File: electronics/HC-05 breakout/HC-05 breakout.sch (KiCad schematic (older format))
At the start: 11 parts, among them SW1 AT?, U1 AMS1117, U2 HC-05

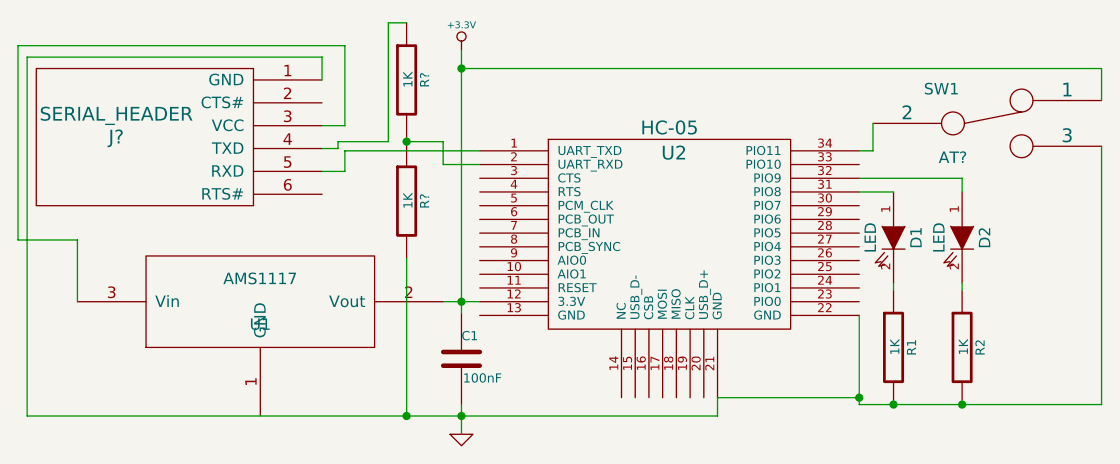
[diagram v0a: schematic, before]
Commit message: annotated hc-05 breakout
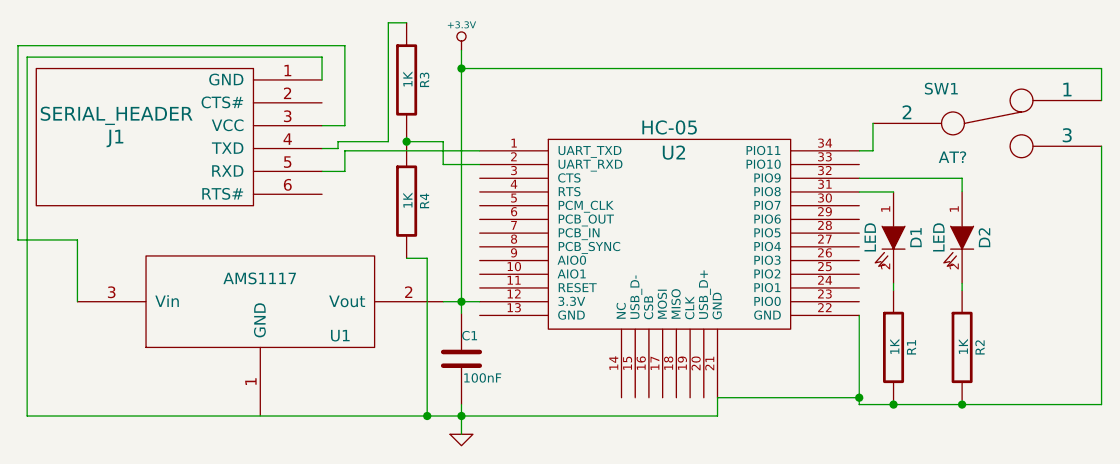
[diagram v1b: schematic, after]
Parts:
- gave numbers to parts that had none: 3
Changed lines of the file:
@@
-$EndComp
-$Comp
-L AMS1117 U1
-U 1 1 533D0877
-P 1900 2220
-F 0 "U1" H 1900 2120 50  0000 C CNN
-F 1 "AMS1117" H 1900 2320 50  0000 C CNN
-F 2 "" H 1900 2220 60  0000 C CNN
-F 3 "" H 1900 2220 60  0000 C CNN
-	1    1900 2220
-	1    0    0    -1
 $EndComp
 $Comp
@@
 Connection ~ 2780 1200
 $Comp
-L SERIAL_HEADER J?
+L SERIAL_HEADER J1
 U 1 1 533D0B24
 P 2170 1050
-F 0 "J?" H 1270 600 60  0000 C CNN
+F 0 "J1" H 1270 600 60  0000 C CNN
 F 1 "SERIAL_HEADER" H 1270 700 60  0000 C CNN
 F 2 "" H 2170 1050 60  0000 C CNN
@@
 	1100 1950 1100 2220
 $Comp
-L R R?
+L R R3
 U 1 1 533D0B4E
 P 2540 1250
-F 0 "R?" V 2620 1250 40  0000 C CNN
+F 0 "R3" V 2620 1250 40  0000 C CNN
 F 1 "1K" V 2547 1251 40  0000 C CNN
 F 2 "~" V 2470 1250 30  0000 C CNN
@@
 $EndComp
 $Comp
-L R R?
+L R R4
 U 1 1 533D0B5D
 P 2540 1780
-F 0 "R?" V 2620 1780 40  0000 C CNN
+F 0 "R4" V 2620 1780 40  0000 C CNN
 F 1 "1K" V 2547 1781 40  0000 C CNN
 F 2 "~" V 2470 1780 30  0000 C CNN
@@
 	2540 1500 2540 1530
 Wire Wire Line
-	2540 2030 2540 2720
-Connection ~ 2540 2720
-Wire Wire Line
 	2540 1520 2700 1520
 Wire Wire Line
@@
 Wire Wire Line
 	880  1150 880  2720
+$Comp
+L AMS1117 U1
+U 1 1 533D0D74
+P 1900 2220
+F 0 "U1" H 2250 2070 50  0000 C CNN
+F 1 "AMS1117" H 1900 2320 50  0000 C CNN
+F 2 "" H 1900 2220 60  0000 C CNN
+F 3 "" H 1900 2220 60  0000 C CNN
+	1    1900 2220
+	1    0    0    -1
+$EndComp
+Wire Wire Line
+	2540 2030 2630 2030
+Wire Wire Line
+	2630 2030 2630 2720
+Connection ~ 2630 2720
 $EndSCHEMATC
